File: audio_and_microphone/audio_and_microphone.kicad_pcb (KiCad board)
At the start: 2 copper layers, 61.2 x 60 mm, 27 parts, among them J1 Conn_01x02, J11 Conn_01x02, J4 Conn_01x02, J5 Conn_01x10_MountingPin, J6 Conn_01x08_MountingPin, J7 Conn_01x08_MountingPin, J8 Conn_01x06_MountingPin, J9 Conn_01x03_Pin

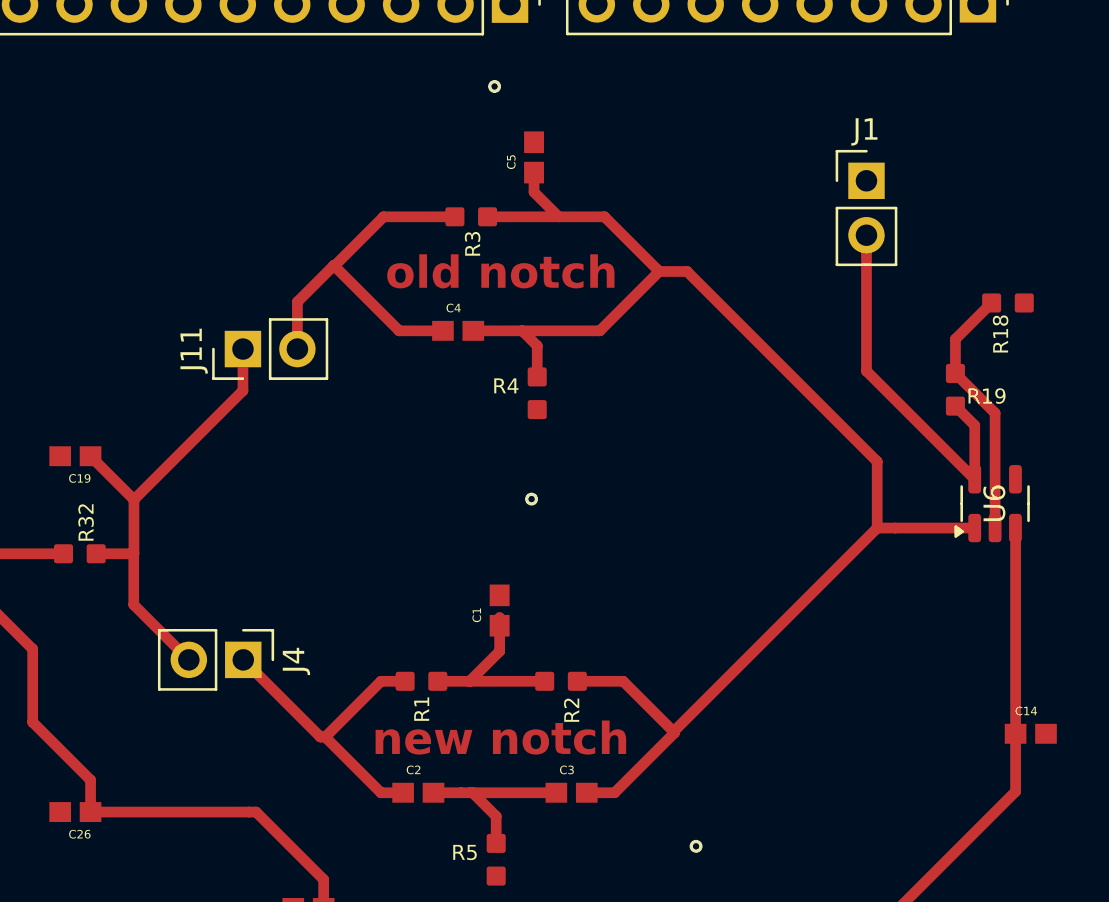
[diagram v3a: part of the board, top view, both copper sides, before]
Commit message: added additional test point and fixed pcb words to be silkscreen
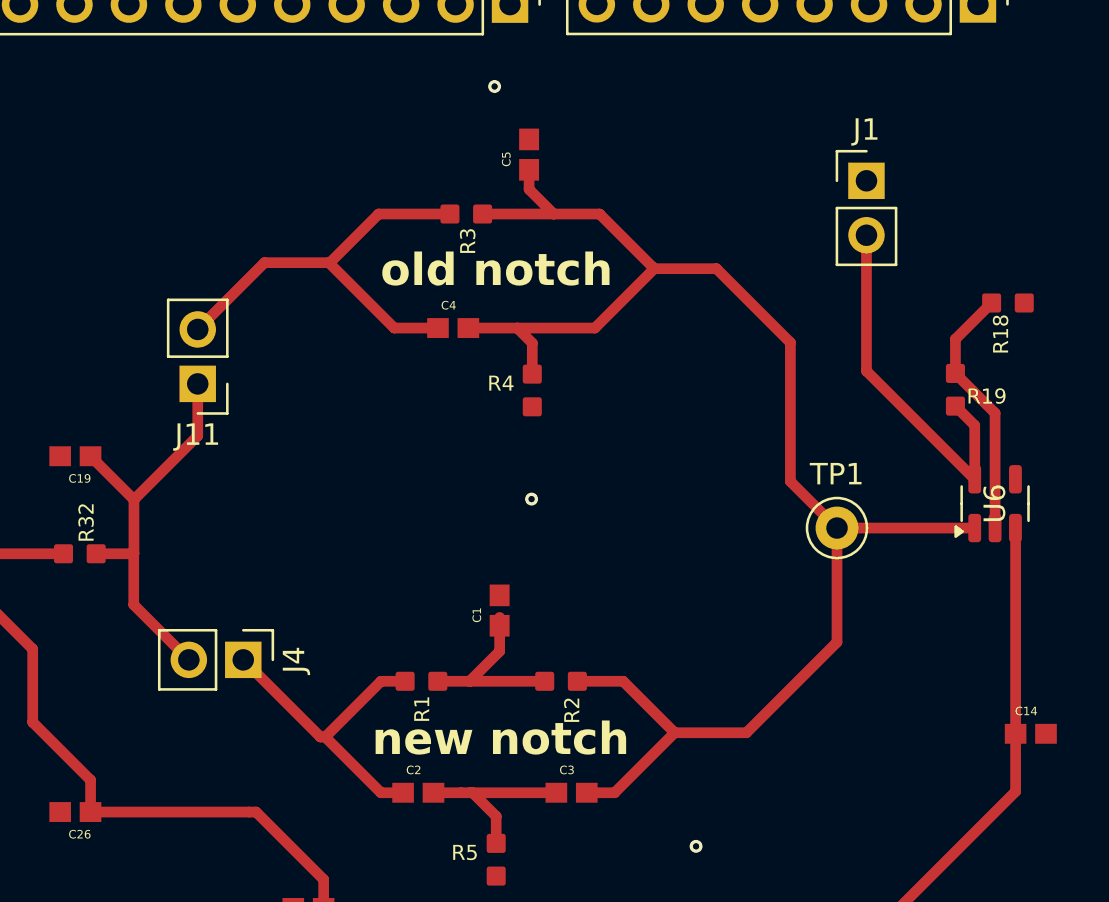
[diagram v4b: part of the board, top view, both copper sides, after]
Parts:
- added TP1: TestPoint, TestPoint:TestPoint_Keystone_5000-5004_Miniature, F.Cu at (81.9, 60.3)
- moved J11 2.66 mm to (52.0, 53.6), turned to 180 degrees
- moved C5 0.26 mm to (67.5, 42.9)
- moved R3 0.26 mm to (64.6, 45.6)
- moved C4 0.26 mm to (64.0, 51.0)
- moved R4 0.26 mm to (67.7, 53.9)
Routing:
- net /new_notch: track 69.6 -> 73.1 mm
- net Net-(J11-Pin_2): track 17.5 -> 20.4 mm
- net /low_pass_filter: track 22.3 -> 19.8 mm
